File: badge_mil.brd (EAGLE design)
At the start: 77.2 x 83.1 mm, 29 parts, among them U1 TINY2313-*S*, X1 FH12-10S-0.5S

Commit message: minor tweaks
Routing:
- net N$13: track 90.6 -> 91.3 mm

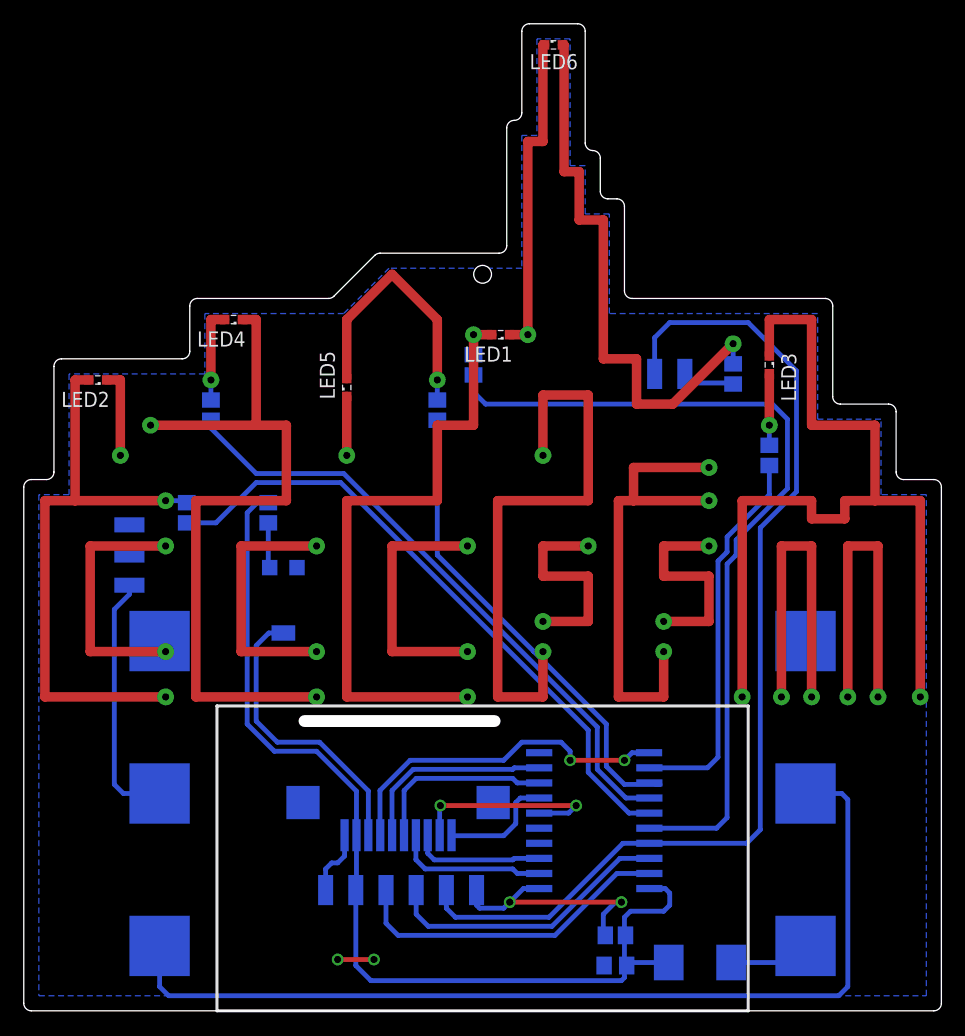
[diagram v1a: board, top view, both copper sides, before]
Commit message: MIC5205 for power supply
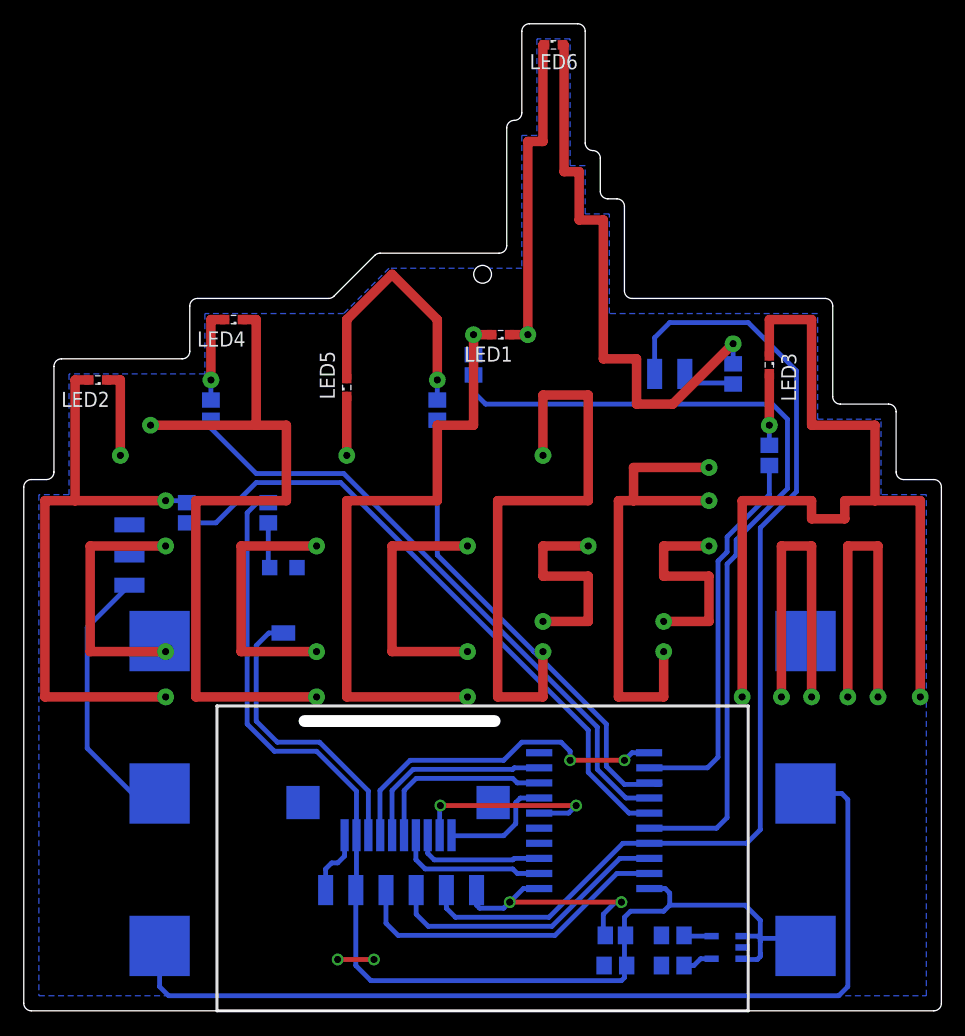
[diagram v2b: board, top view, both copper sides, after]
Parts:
- removed D1: LL 5819, diode:MELF-MLL41
- added C2: 470 pF, rcl:C0805
- added C3: 2,2 µF, rcl:C0805
- added U2: (no value), SparkFun-PowerIC:SOT23-5
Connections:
- new net N$28: C2.2, U2.4
- net GND: now also C2.1, C3.1, U2.2
- net N$37: now also C3.2, U2.5; no longer D1.A, U$1.V+1, U$1.V+2
- net VCC: now also U$1.V+1, U$1.V+2, U2.1, U2.3; no longer D1.C
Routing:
- net VCC: track 86.7 -> 101.6 mm
- net N$37: track 6.84 -> 2.39 mm
- net N$28: track 0.00 -> 2.56 mm
- net N$23: track 21.4 -> 22.9 mm

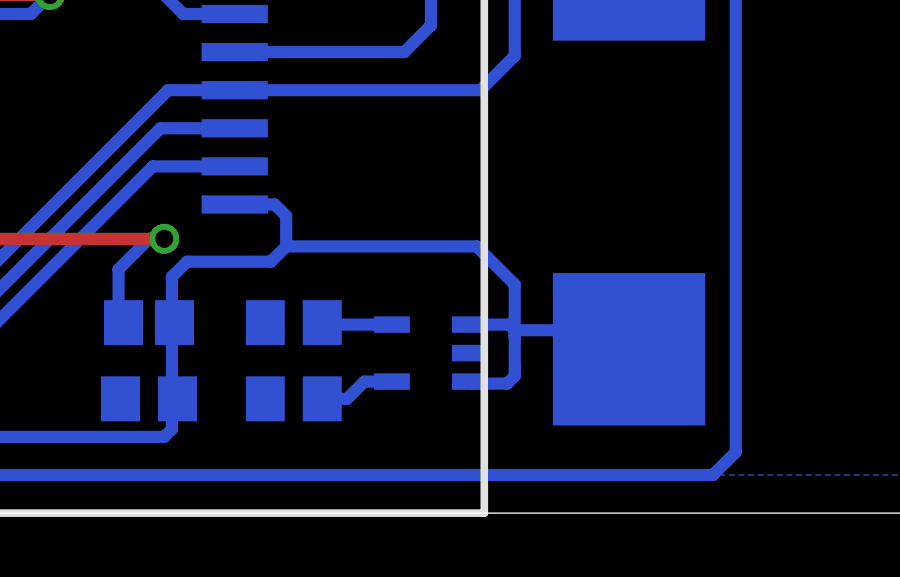
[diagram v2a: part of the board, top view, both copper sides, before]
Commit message: fix short circuit
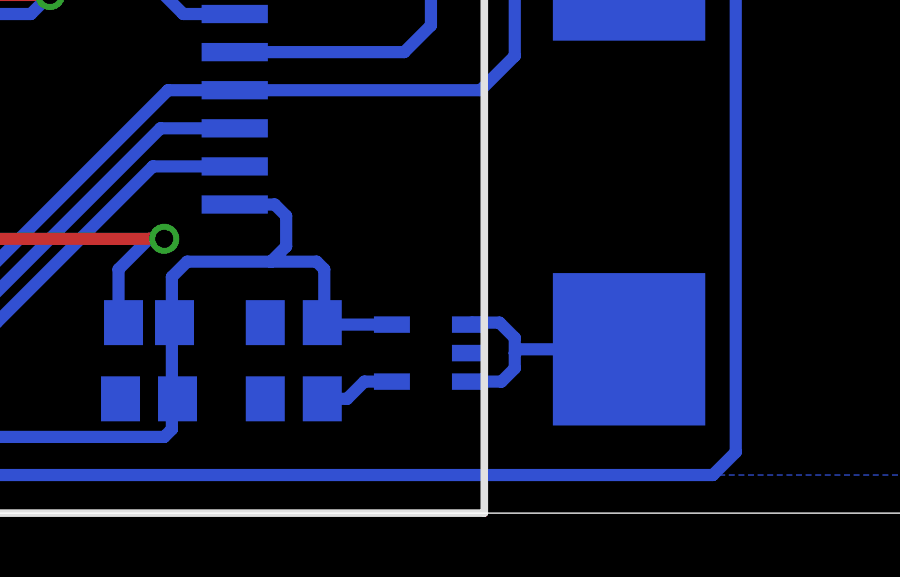
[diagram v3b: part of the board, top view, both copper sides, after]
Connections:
- removed net N$37: C3.2, U2.5
- new net N$29: U$1.V+1, U$1.V+2, U2.1, U2.3
- net VCC: now also C3.2, U2.5; no longer U$1.V+1, U$1.V+2, U2.1, U2.3
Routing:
- net VCC: track 101.6 -> 89.0 mm
- net N$29: track 0.00 -> 8.29 mm
- net N$37: track 2.39 -> 0.00 mm
